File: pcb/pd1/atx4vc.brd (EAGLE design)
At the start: 86 x 70 mm, 76 parts, among them IC2 REG1117, IC3 STM32F042F4, IC4 MY_7905DT, J1 ATX24RH, SW1 324_SW, SW2 324_SW, SW3 324_SW, SW4 324_SW, SW5 324_SW, SW7 324_SW, U1 USBC_16P, U2 USBC_16P

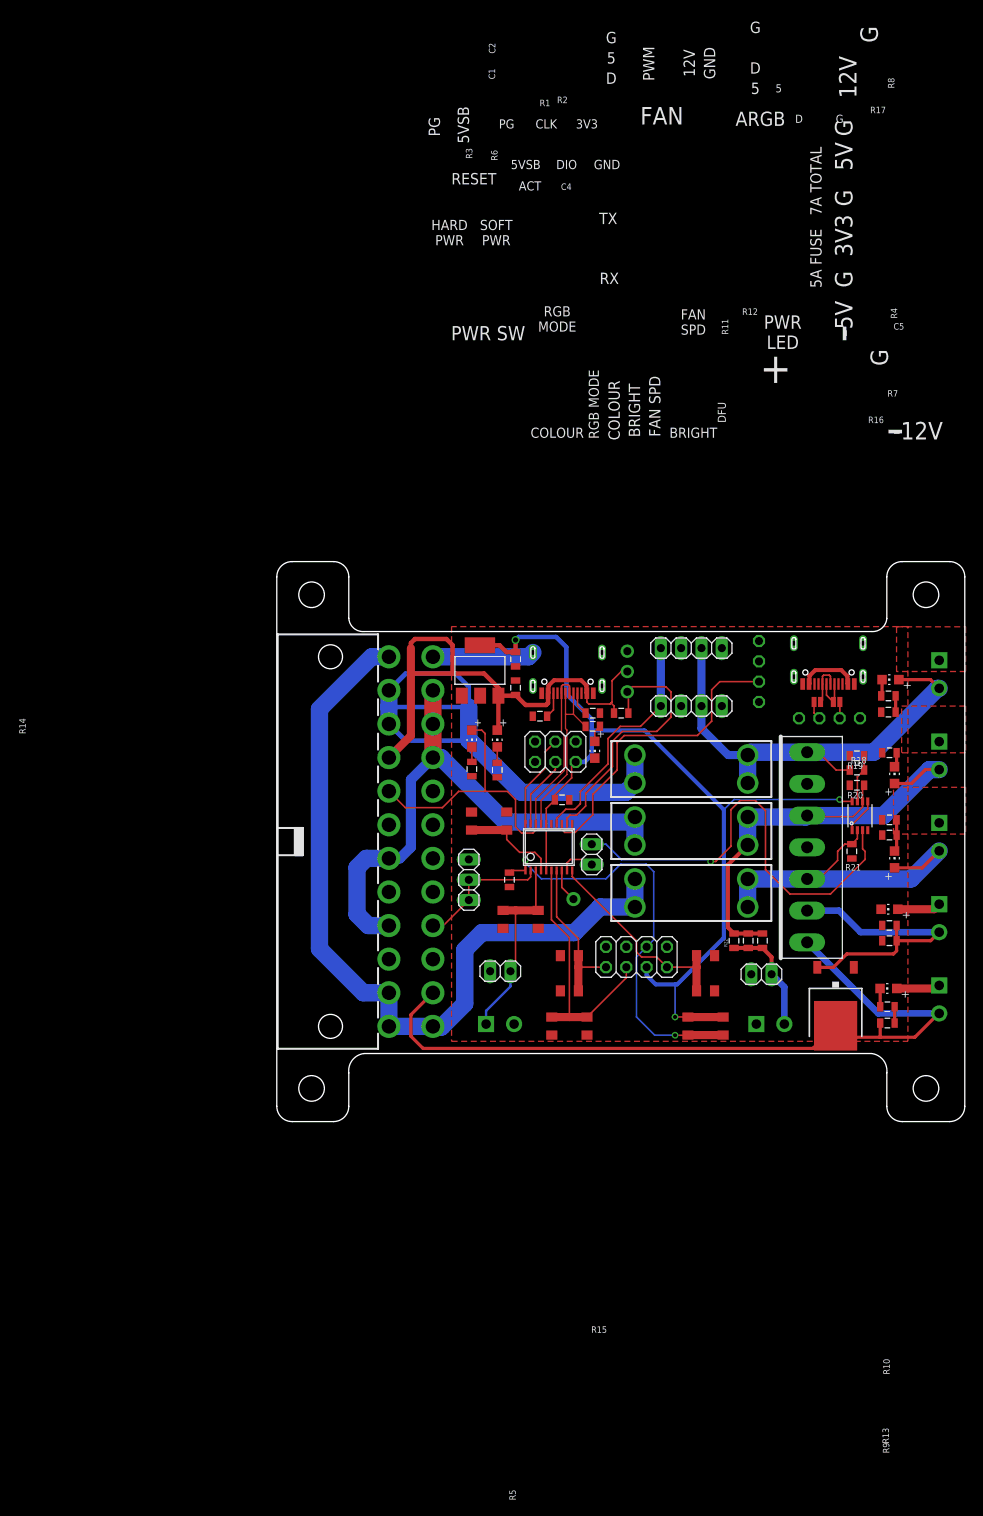
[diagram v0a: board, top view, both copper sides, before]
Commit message: adding power connector and fuse detect
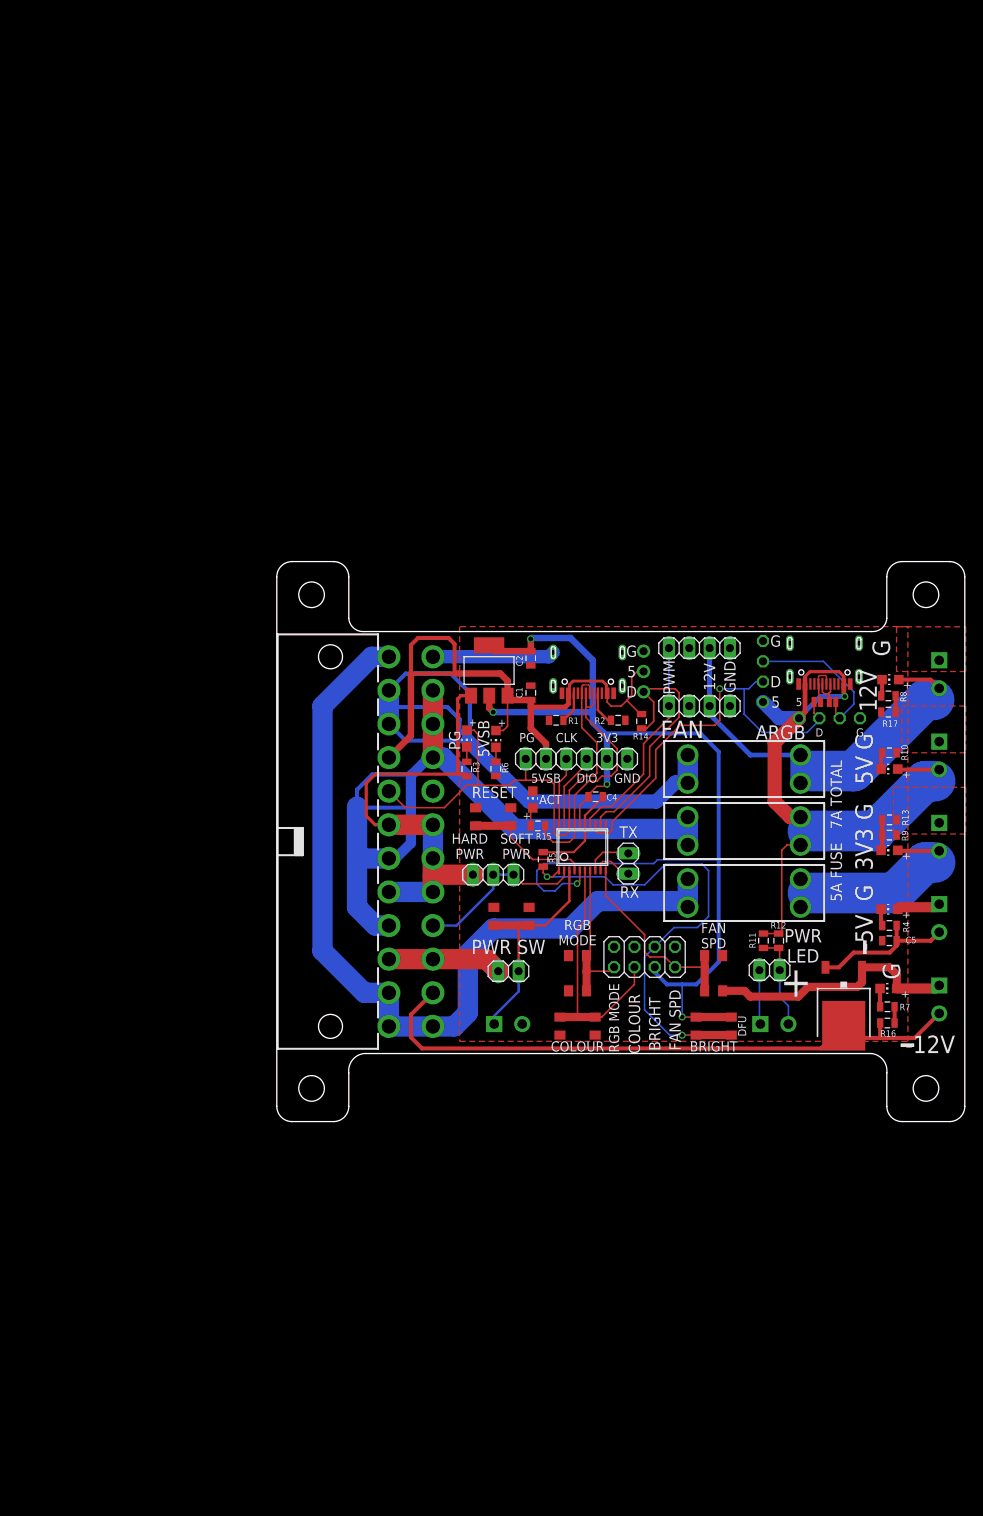
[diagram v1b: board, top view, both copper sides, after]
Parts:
- removed JP15: (no value), pinhead:2X03
- removed R18, R19, R20, R21, R22: 5K1, atx_power_control:0805
- removed U$4: VH396, 396_conn:396_7P
- removed U$6: 74LVC2G08SSOP8, atx4vc:SSOP08
- added JP8: (no value), atx_power_control:1X04
- JP10: device adafruit:1X01-CLEANBIG -> pinhead:1X02
- moved R15 14.2 mm to (32.6, 37.0), turned to 180 degrees
- moved JP3 13.8 mm to (32.4, 45.3), turned to 0 degrees
- moved LED8 9.94 mm to (32.0, 40.3), turned to 0 degrees
- moved JP10 8.17 mm to (43.9, 32.3), turned to 270 degrees
- moved U$5 6.60 mm to (58.4, 44.1)
- moved U$7 6.60 mm to (58.4, 28.6)
- moved U$8 6.60 mm to (58.4, 36.3)
- moved R5 4.93 mm to (33.3, 32.8), turned to 270 degrees
- moved C4 4.21 mm to (39.9, 40.6)
- moved IC3 4.19 mm to (38.2, 34.3)
- moved R2 3.30 mm to (42.7, 50.2)
- moved JP5 3.11 mm to (27.1, 30.9), turned to 180 degrees
- moved R14 2.74 mm to (45.6, 50.0), turned to 90 degrees
- moved U2 2.54 mm to (38.9, 57.4)
- moved R1 2.09 mm to (34.9, 50.2)
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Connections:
- removed net N$24: JP3.2, U$6.3
- removed net N$38: IC3.9, JP3.1
- removed net N$39: R18.2, R19.1, U$6.7
- net +3V3: now also JP8.3; no longer JP15.5, U$6.8
- net GND: now also JP8.4; no longer JP15.6, R19.2, R20.2, R21.1, U$4.P$4, U$4.P$6, U$6.4
- net N$11: no longer U$4.P$2
- net N$12: now also IC3.9, JP10.2; no longer U$6.1, U$6.5
- net N$15: no longer R18.1, U$4.P$7
- net N$16: no longer R21.2, U$4.P$3, U$6.2
- net N$17: no longer R22.1
- net N$2: no longer U$4.P$1
- net N$3: now also JP8.1; no longer JP15.4
- net N$30: no longer R20.1, R22.2, U$4.P$5, U$6.6
- net N$4: now also JP8.2; no longer JP15.3
- net PG: now also JP3.1
- net VCC: now also JP3.2
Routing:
- net GND: track 23.6 -> 151.7 mm
- net N$24: track 55.6 -> 0.00 mm, vias 1 -> 0
- net N$10: track 71.3 -> 101.2 mm
- net +3V3: track 122.5 -> 148.7 mm, vias 3 -> 5
- net N$2: track 98.2 -> 78.3 mm
- net N$11: track 37.3 -> 18.3 mm
- net N$30: track 69.8 -> 87.4 mm, vias 0 -> 1
- net N$37: track 2.04 -> 19.2 mm
- net N$16: track 45.4 -> 30.0 mm
- net VCC: track 68.1 -> 81.3 mm
- net N$21: track 70.8 -> 81.0 mm
- net PG: track 55.1 -> 65.2 mm
- net N$35: track 41.4 -> 51.5 mm, vias 0 -> 1
- net USB_DN: track 23.5 -> 32.7 mm
- net BUTTON2: track 52.7 -> 59.9 mm
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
